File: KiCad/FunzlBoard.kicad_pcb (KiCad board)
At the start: 2 copper layers, 174 x 149 mm, 65 parts, among them SW1 SW_MEC_5E, SW2 SW_MEC_5E, SW3 SW_MEC_5E, SW4 SW_MEC_5E, SW5 SW_MEC_5E, U1 ESP32-C3_SUPERMINI_SMD, U2 ADS7828, U3 MCP23017_SO

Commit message: Add connectors
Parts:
- added 1WI1: Banana Plug Cable, TerminalBlock_Phoenix:TerminalBlock_Phoenix_MPT-0,5-3-2.54_1x03_P2.54mm_Horizontal, B.Cu at (35.5, 36.0)
- added C1: 470µF, Capacitor_THT:CP_Radial_D6.3mm_P2.50mm, B.Cu at (138.0, 9.00)
- added C2: 330µF, Capacitor_THT:CP_Radial_D6.3mm_P2.50mm, B.Cu at (20.5, 109.0)
- added C3: 330µF, Capacitor_THT:CP_Radial_D6.3mm_P2.50mm, B.Cu at (161.5, 112.0)
- added J1: Poti, Lib:Connector3, B.Cu at (69.8, 118.3)
- added J10: Slider, Lib:Connector2, B.Cu at (17.7, 94.0)
- added J11: Toggle, Lib:Connector2, B.Cu at (120.7, 39.0)
- added J12: Button Small, Lib:Connector2, B.Cu at (38.7, 104.0)
- added J13: Virb.1, Lib:Connector2, B.Cu at (9.00, 123.0)
- added J14: Vibr.2, Lib:Connector2, B.Cu at (171.0, 123.0)
- added J15: 5V IN, Lib:Connector2, B.Cu at (164.3, 18.0)
- added J16: BAT, Lib:Connector2, B.Cu at (158.7, 9.00)
- added J17: LED G, Lib:Connector2, B.Cu at (145.0, 73.3)
- added J18: LED R, Lib:Connector2, B.Cu at (131.0, 39.0)
- added J19: PWR Switch, Lib:Connector2, B.Cu at (139.0, 17.7)
- added J2: Banana Plug Socket 1, Connector_PinHeader_2.54mm:PinHeader_1x01_P2.54mm_Horizontal, B.Cu at (28.0, 65.0)
- added J20: BAT Monitor, Lib:Connector2, B.Cu at (136.7, 93.0)
- added J21: LED Blink, Lib:Connector2, B.Cu at (148.3, 93.0)
- added J22: BZ 1, Lib:Connector2, B.Cu at (31.3, 8.00)
- added J23: BZ 2, Lib:Connector2, B.Cu at (94.3, 6.00)
- added J24: BZ 3, Lib:Connector2, B.Cu at (146.7, 8.00)
- added J3: Banana Plug Socket 2, Connector_PinHeader_2.54mm:PinHeader_1x01_P2.54mm_Horizontal, B.Cu at (46.0, 65.0)
- added J4: Banana Plug Socket 3, Connector_PinHeader_2.54mm:PinHeader_1x01_P2.54mm_Horizontal, B.Cu at (64.0, 65.0)
- added J5: 3-Way, Lib:Connector3, B.Cu at (135.5, 112.0)
- added J6: 2-Way 1, Lib:Connector2, B.Cu at (69.0, 140.0)
- added J7: 2-Way 2, Lib:Connector2, B.Cu at (49.0, 140.0)
- added J8: 2-Way 3, Lib:Connector2, B.Cu at (29.0, 140.0)
- added J9: Rocker, Lib:Connector2, B.Cu at (123.7, 130.0)
- added Q1: 2N7002, Package_TO_SOT_SMD:SOT-23, F.Cu at (12.1, 117.0)
- added Q2: 2N7002, Package_TO_SOT_SMD:SOT-23, F.Cu at (169.1, 117.0)
- added R1: 220R, Resistor_SMD:R_1206_3216Metric, B.Cu at (21.0, 13.0)
- added R2: 33R, Resistor_SMD:R_1206_3216Metric, B.Cu at (4.71, 12.4)
- added R3: 33R, Resistor_SMD:R_1206_3216Metric, B.Cu at (16.0, 6.00)
- added R4: 33R, Resistor_SMD:R_1206_3216Metric, B.Cu at (16.0, 13.0)
- added TP1: GPIO5, TestPoint:TestPoint_THTPad_D1.5mm_Drill0.7mm, B.Cu at (14.0, 113.0)
- added TP2: GPIO6, TestPoint:TestPoint_THTPad_D1.5mm_Drill0.7mm, B.Cu at (166.0, 113.0)
- added U4: ~, Lib:Battery_Management, B.Cu at (153.6, 31.5)
- SW1: value SW_MEC_5E -> Button R
- SW2: value SW_MEC_5E -> Button Y
- SW3: value SW_MEC_5E -> Button G
- SW4: value SW_MEC_5E -> Button B
- turned D26 to -112.5 degrees
- turned D27 to -67.5 degrees
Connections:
- SW1 pad 1: Net-(U3-GPB0) -> Net-(SW1-Pad1)
- SW1 pad 2: Net-(U3-GPB0) -> Net-(SW1-Pad1)
- SW2 pad 1: Net-(U3-GPB1) -> Net-(SW2-Pad1)
- SW2 pad 2: Net-(U3-GPB1) -> Net-(SW2-Pad1)
- SW3 pad 1: Net-(U3-GPB2) -> Net-(SW3-Pad1)
- SW3 pad 2: Net-(U3-GPB2) -> Net-(SW3-Pad1)
- SW4 pad 1: Net-(U3-GPB3) -> Net-(SW4-Pad1)
- SW4 pad 2: Net-(U3-GPB3) -> Net-(SW4-Pad1)
- SW5 pad 1: Net-(U3-GPB4) -> Net-(J16-Pin_1)
- SW5 pad 2: Net-(U3-GPB4) -> Net-(J16-Pin_1)
- SW5 pad 3: GND -> Net-(SW5-A)
- SW5 pad 4: GND -> Net-(SW5-A)
- U1 pad 0: unconnected-(U1-GPIO0-Pad0) -> Net-(U1-GPIO0)
- U1 pad 1: unconnected-(U1-GPIO1-Pad1) -> Net-(U1-GPIO1)
- U1 pad 2: Net-(D1-DIN) -> Net-(U1-GPIO2)
- U1 pad 3: unconnected-(U1-GPIO3-Pad3) -> Net-(D1-DIN)
- U1 pad 4: unconnected-(U1-GPIO4-Pad4) -> Net-(U1-GPIO4)
- U1 pad 5: unconnected-(U1-GPIO5-Pad5) -> Net-(Q1-G)
- U1 pad 6: unconnected-(U1-GPIO6-Pad6) -> Net-(Q2-G)
- U3 pad 1: Net-(U3-GPB0) -> Net-(J5-Pin_1)
- U3 pad 2: Net-(U3-GPB1) -> Net-(J5-Pin_3)
- U3 pad 25: unconnected-(U3-GPA4-Pad25) -> Net-(J12-Pin_2)
- U3 pad 26: unconnected-(U3-GPA5-Pad26) -> Net-(J2-Pin_1)
- U3 pad 27: unconnected-(U3-GPA6-Pad27) -> Net-(J3-Pin_1)
- U3 pad 28: unconnected-(U3-GPA7-Pad28) -> Net-(J4-Pin_1)
- U3 pad 3: Net-(U3-GPB2) -> Net-(J6-Pin_2)
- U3 pad 4: Net-(U3-GPB3) -> Net-(J7-Pin_2)
- U3 pad 5: Net-(U3-GPB4) -> Net-(J8-Pin_2)
- U3 pad 6: unconnected-(U3-GPB5-Pad6) -> Net-(J9-Pin_2)
- U3 pad 7: unconnected-(U3-GPB6-Pad7) -> Net-(J10-Pin_2)
- U3 pad 8: unconnected-(U3-GPB7-Pad8) -> Net-(J11-Pin_2)
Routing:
- net Net-(D1-DIN): track 13.6 -> 0.00 mm
- net Net-(D27-DOUT): track 28.0 -> 31.4 mm
- net GND: vias 17 -> 16
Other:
- board text added: "+"
- board text added: "-"

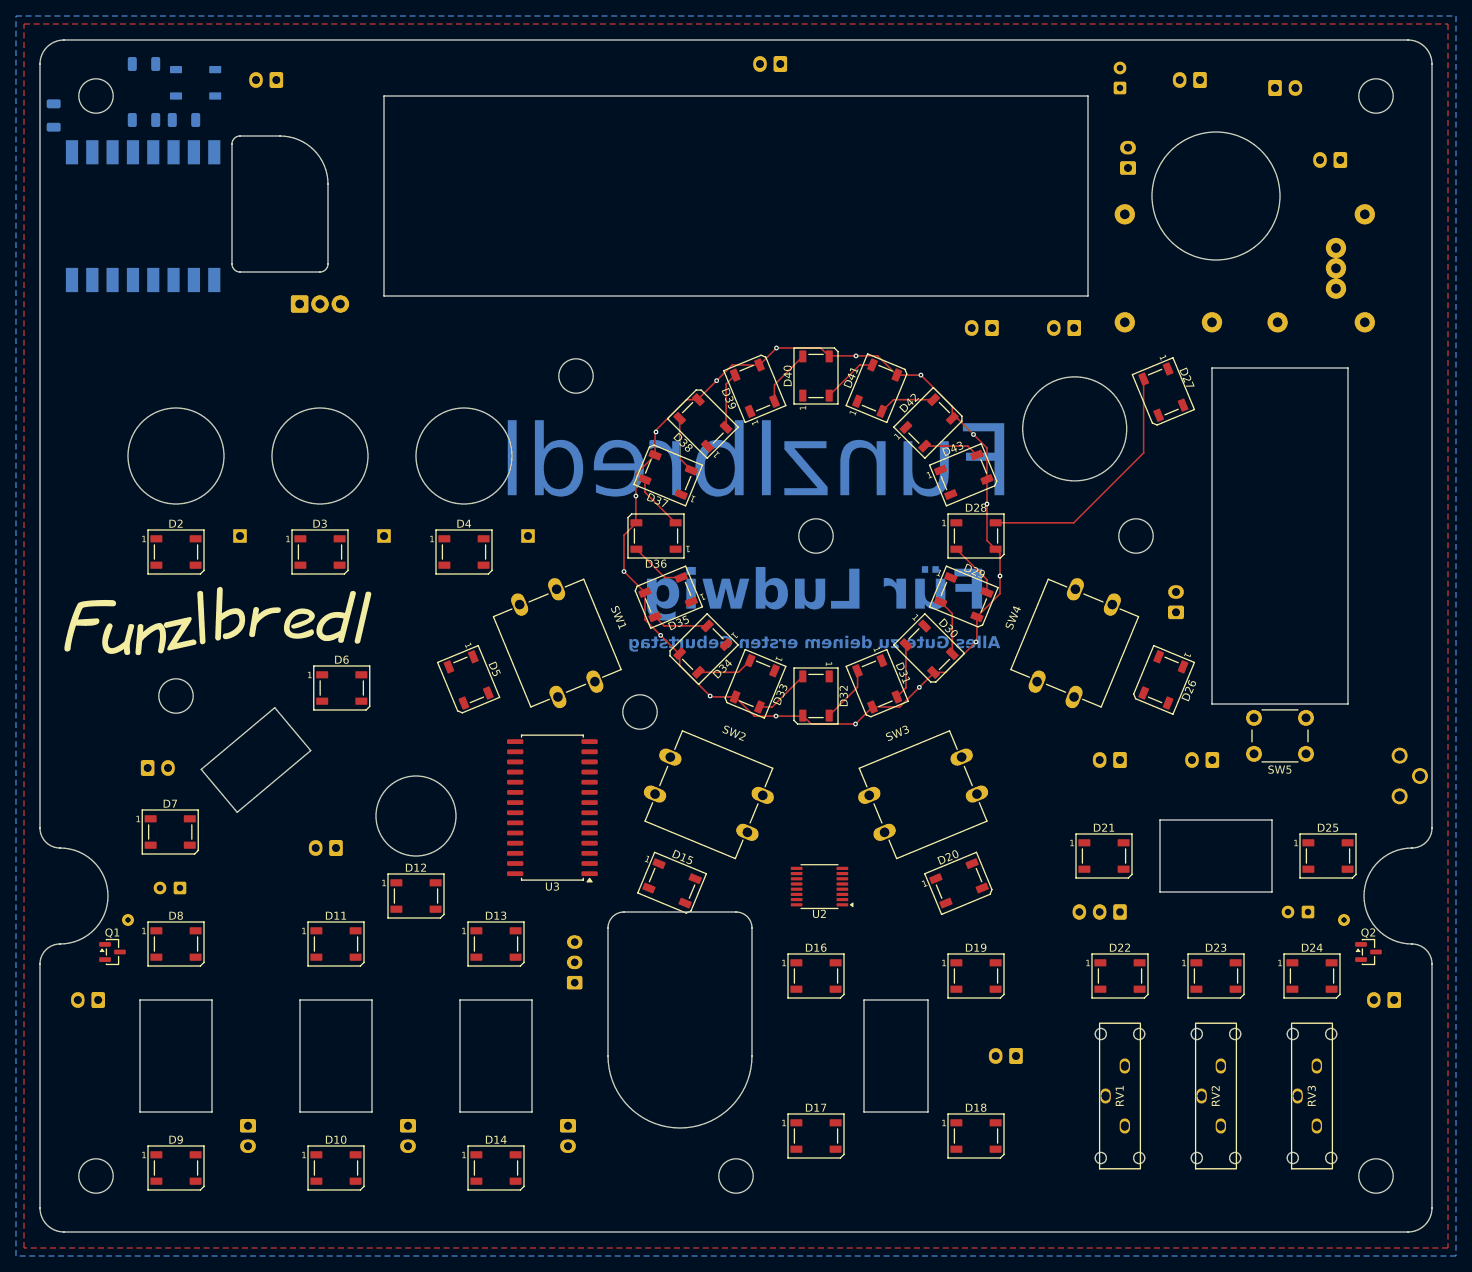
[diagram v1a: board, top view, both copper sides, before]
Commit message: Add 2nd trimmer
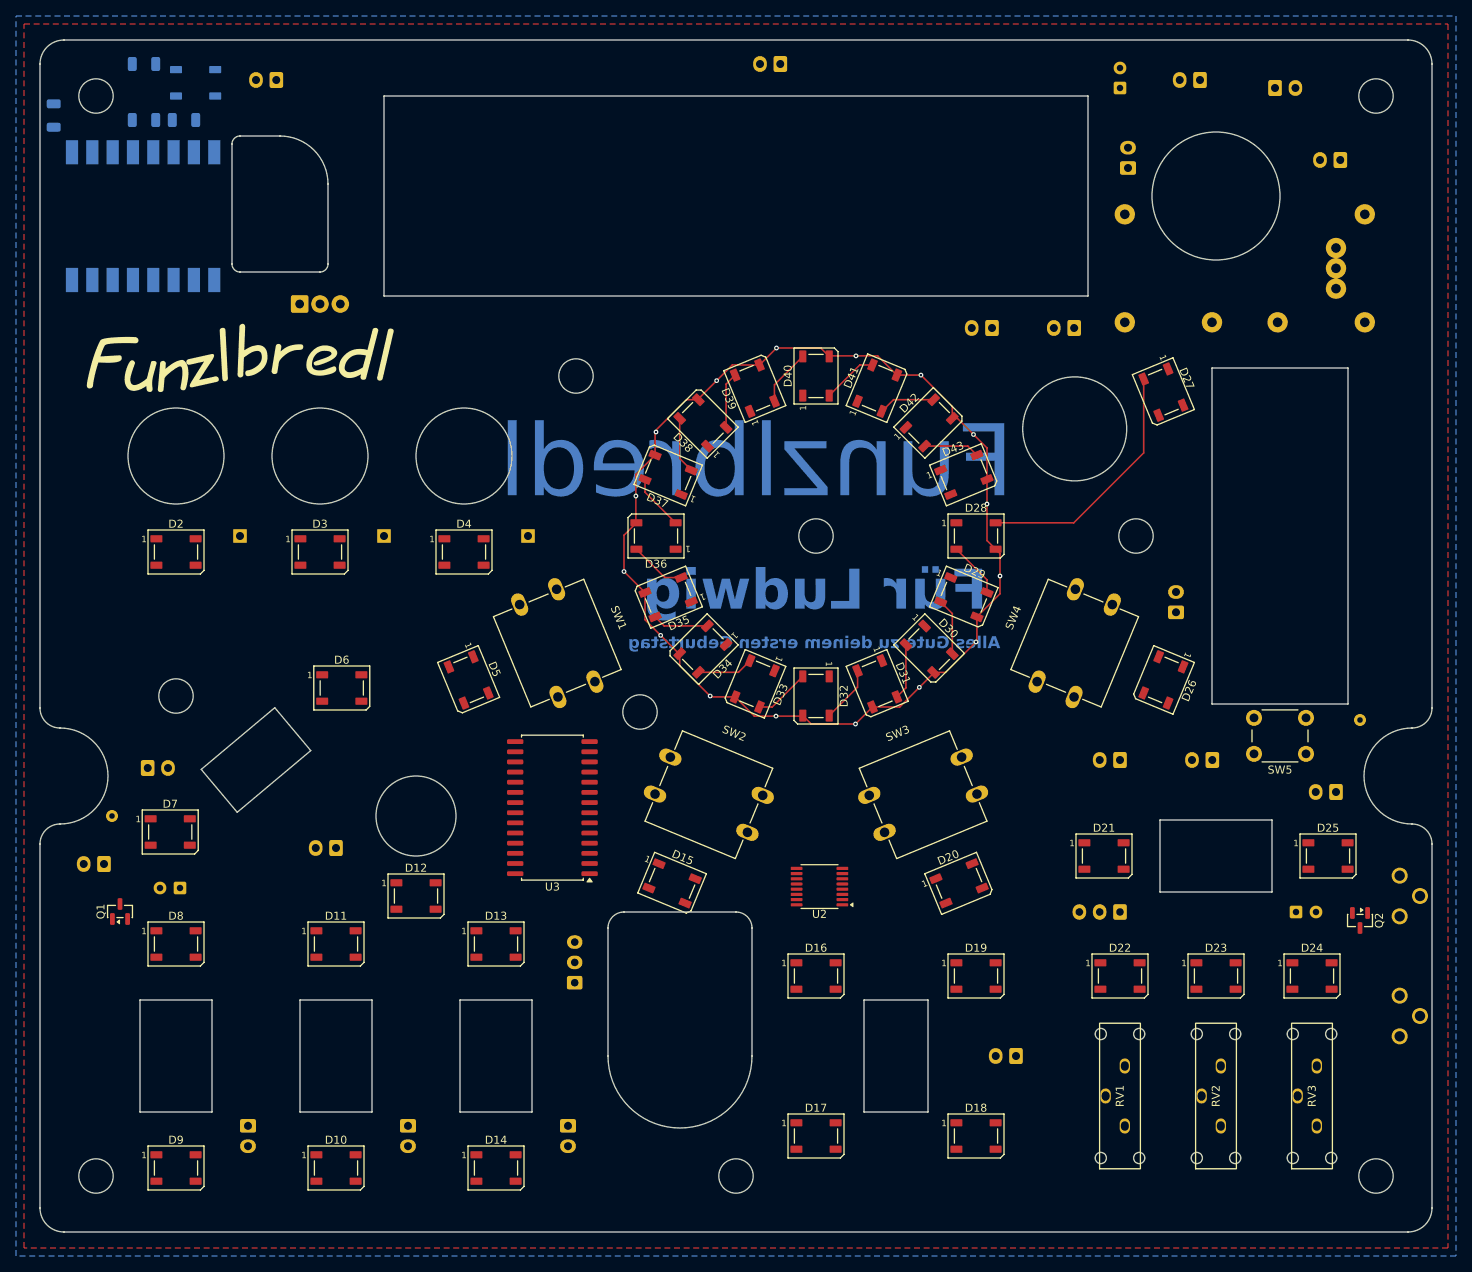
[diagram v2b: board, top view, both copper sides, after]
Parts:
- added RV4: R_Potentiometer, Lib:TrimmerH, B.Cu at (175.3, 125.0)
- moved J14 27.0 mm to (163.7, 97.0)
- moved TP2 25.1 mm to (168.0, 88.0)
- moved J13 17.0 mm to (9.73, 106.0)
- moved RV5 15.0 mm to (175.3, 110.0)
- moved TP1 13.2 mm to (12.0, 100.0)
- moved Q1 5.15 mm to (13.0, 111.9), turned to 90 degrees
- moved Q2 4.08 mm to (168.0, 113.1), turned to -90 degrees
- moved C3 1.50 mm to (160.0, 112.0), turned to 0 degrees
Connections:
- U2 pad 6: unconnected-(U2-CH5-Pad6) -> Net-(U2-CH5)
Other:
- outline, holes or cut-outs redrawn

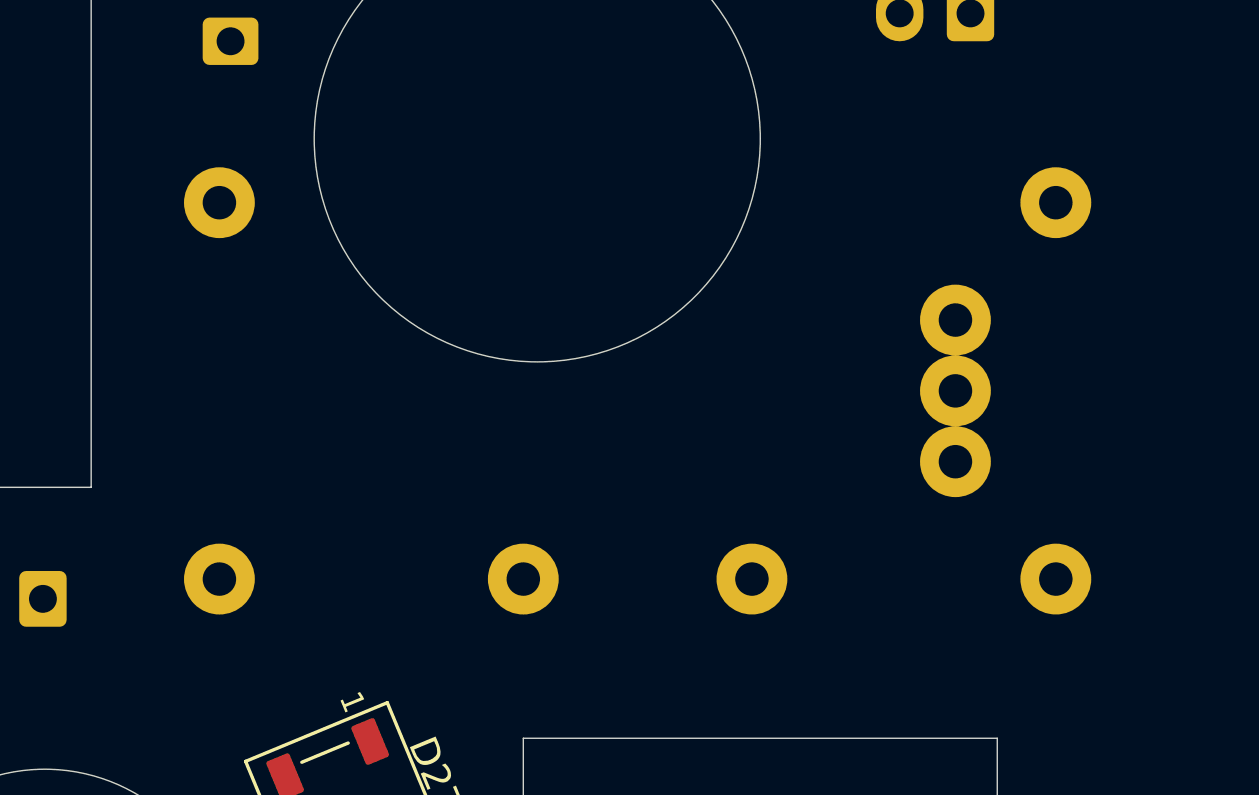
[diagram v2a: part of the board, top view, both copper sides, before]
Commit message: Add Battery Management to OpenSCAD
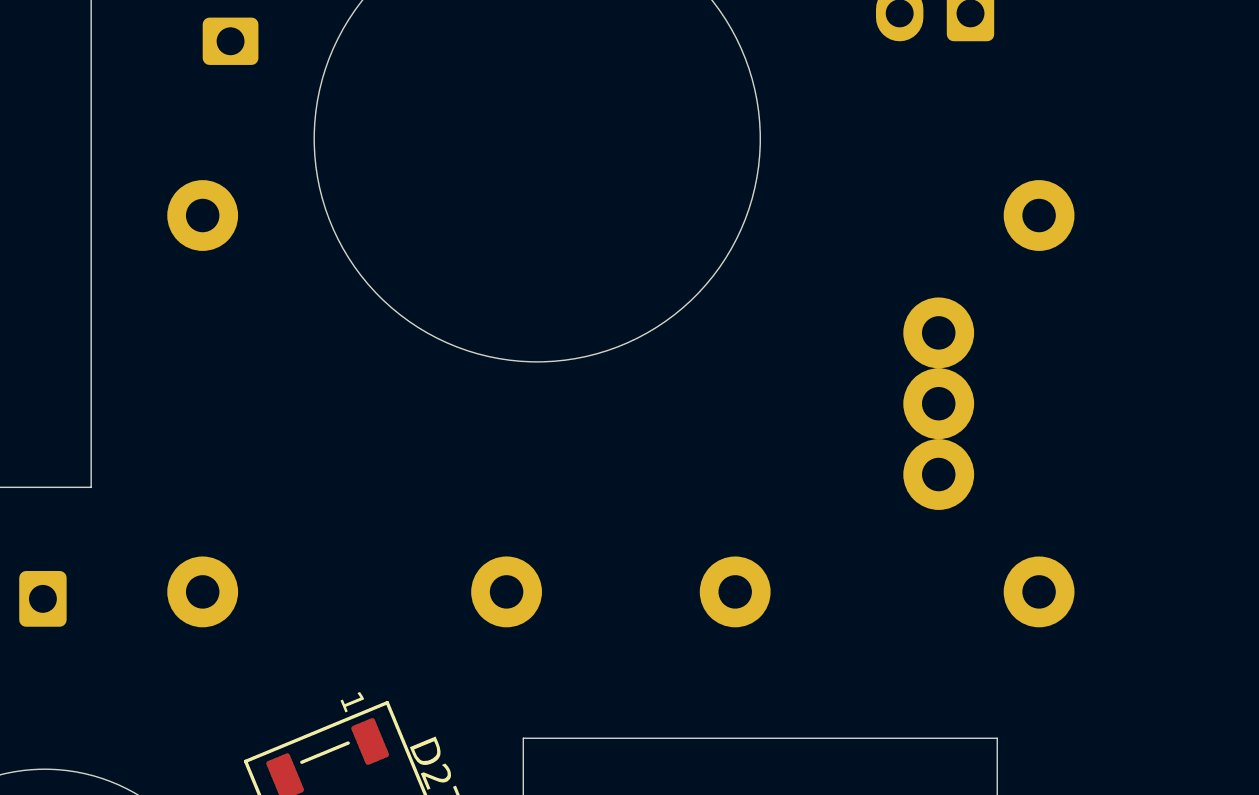
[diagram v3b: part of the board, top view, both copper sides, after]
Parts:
- moved U4 0.76 mm to (153.0, 32.0)
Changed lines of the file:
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@@
 	(footprint "Lib:Battery_Management"
 		(layer "B.Cu")
-		(at 153.6 31.54 180)
+		(at 153 32 180)
 		(property "Reference" "U4"
 			(at 0 0.5 0)

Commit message: Place capas
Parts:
- added C10: 100nF, Capacitor_SMD:C_1206_3216Metric, F.Cu at (144.0, 38.0)
- added C11: 100nF, Capacitor_SMD:C_1206_3216Metric, F.Cu at (140.0, 91.0)
- added C12: 100nF, Capacitor_SMD:C_1206_3216Metric, F.Cu at (173.0, 104.0)
- added C13: 100nF, Capacitor_SMD:C_1206_3216Metric, F.Cu at (149.0, 114.0)
- added C14: 100nF, Capacitor_SMD:C_1206_3216Metric, F.Cu at (161.4, 113.6)
- added C15: 100nF, Capacitor_SMD:C_1206_3216Metric, F.Cu at (128.5, 105.0)
- added C16: 100nF, Capacitor_SMD:C_1206_3216Metric, F.Cu at (100.5, 126.0)
- added C17: 100nF, Capacitor_SMD:C_1206_3216Metric, F.Cu at (121.0, 126.0)
- added C18: 100nF, Capacitor_SMD:C_1206_3216Metric, F.Cu at (101.0, 146.0)
- added C19: 100nF, Capacitor_SMD:C_1206_3216Metric, F.Cu at (120.5, 146.0)
- added C20: 100nF, Capacitor_SMD:C_1206_3216Metric, F.Cu at (124.0, 114.0)
- added C21: 100nF, Capacitor_SMD:C_1206_3216Metric, F.Cu at (89.0, 111.0)
- added C22: 100nF, Capacitor_SMD:C_1206_3216Metric, F.Cu at (50.0, 116.0)
- added C23: 100nF, Capacitor_SMD:C_1206_3216Metric, F.Cu at (60.0, 121.7)
- added C24: 100nF, Capacitor_SMD:C_1206_3216Metric, F.Cu at (40.0, 121.7)
- added C25: 100nF, Capacitor_SMD:C_1206_3216Metric, F.Cu at (20.5, 121.7)
- added C26: 100nF, Capacitor_SMD:C_1206_3216Metric, F.Cu at (20.5, 150.0)
- added C27: 100nF, Capacitor_SMD:C_1206_3216Metric, F.Cu at (40.5, 150.0)
- added C28: 100nF, Capacitor_SMD:C_1206_3216Metric, F.Cu at (60.5, 150.0)
- added C29: 100nF, Capacitor_SMD:C_1206_3216Metric, F.Cu at (42.0, 90.0)
- added C30: 100nF, Capacitor_SMD:C_1206_3216Metric, F.Cu at (52.5, 91.0)
- added C31: 100nF, Capacitor_SMD:C_1206_3216Metric, F.Cu at (124.3, 75.1)
- added C32: 100nF, Capacitor_SMD:C_1206_3216Metric, F.Cu at (118.6, 83.8)
- added C33: 100nF, Capacitor_SMD:C_1206_3216Metric, F.Cu at (137.0, 114.5)
- added C34: 100nF, Capacitor_SMD:C_1206_3216Metric, F.Cu at (49.0, 64.0)
- added C35: 100nF, Capacitor_SMD:C_1206_3216Metric, F.Cu at (31.0, 63.0)
- added C36: 100nF, Capacitor_SMD:C_1206_3216Metric, F.Cu at (100.1, 91.2)
- added C37: 100nF, Capacitor_SMD:C_1206_3216Metric, F.Cu at (73.5, 65.0)
- added C38: 100nF, Capacitor_SMD:C_1206_3216Metric, F.Cu at (81.5, 46.7)
- added C39: 100nF, Capacitor_SMD:C_1206_3216Metric, F.Cu at (118.4, 46.4)
- added C4: 100nF, Capacitor_SMD:C_1206_3216Metric, F.Cu at (95.0, 110.0)
- added C40: 100nF, Capacitor_SMD:C_1206_3216Metric, F.Cu at (124.4, 55.1)
- added C41: 100nF, Capacitor_SMD:C_1206_3216Metric, F.Cu at (110.1, 89.2)
- added C42: 100nF, Capacitor_SMD:C_1206_3216Metric, F.Cu at (81.6, 83.6)
- added C43: 100nF, Capacitor_SMD:C_1206_3216Metric, F.Cu at (90.0, 41.0)
- added C44: 100nF, Capacitor_SMD:C_1206_3216Metric, F.Cu at (110.1, 40.8)
- added C45: 100nF, Capacitor_SMD:C_1206_3216Metric, F.Cu at (126.2, 65.0)
- added C46: 100nF, Capacitor_SMD:C_1206_3216Metric, F.Cu at (89.8, 89.1)
- added C47: 100nF, Capacitor_SMD:C_1206_3216Metric, F.Cu at (75.6, 74.9)
- added C48: 100nF, Capacitor_SMD:C_1206_3216Metric, F.Cu at (75.9, 55.0)
- added C49: 100nF, Capacitor_SMD:C_1206_3216Metric, F.Cu at (100.1, 38.9)
- added C5: 100nF, Capacitor_SMD:C_1206_3216Metric, F.Cu at (75.0, 95.5)
- added C6: 330µF, Capacitor_THT:CP_Radial_D6.3mm_P2.50mm, B.Cu at (59.5, 42.0)
- added C7: 330µF, Capacitor_THT:CP_Radial_D6.3mm_P2.50mm, B.Cu at (41.0, 11.5)
- added C8: 100nF, Capacitor_SMD:C_1206_3216Metric, F.Cu at (21.0, 73.0)
- added C9: 100nF, Capacitor_SMD:C_1206_3216Metric, F.Cu at (20.0, 107.0)
- added R5: 4K7, Resistor_SMD:R_1206_3216Metric, F.Cu at (100.5, 100.3)
- added R6: 4K7, Resistor_SMD:R_1206_3216Metric, F.Cu at (100.5, 96.0)
- moved J20 38.8 mm to (144.7, 55.0)
- moved C2 2.50 mm to (18.0, 109.0), turned to 0 degrees
- turned D21 to 180 degrees
- turned D22 to 180 degrees
- turned D23 to 180 degrees
- turned D3 to 180 degrees
- turned D4 to 180 degrees
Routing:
- net GND: track 156.4 -> 64.5 mm
- net Net-(D27-DOUT): track 31.4 -> 30.4 mm
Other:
- outline, holes or cut-outs redrawn
